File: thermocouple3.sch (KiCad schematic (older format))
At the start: 2 parts

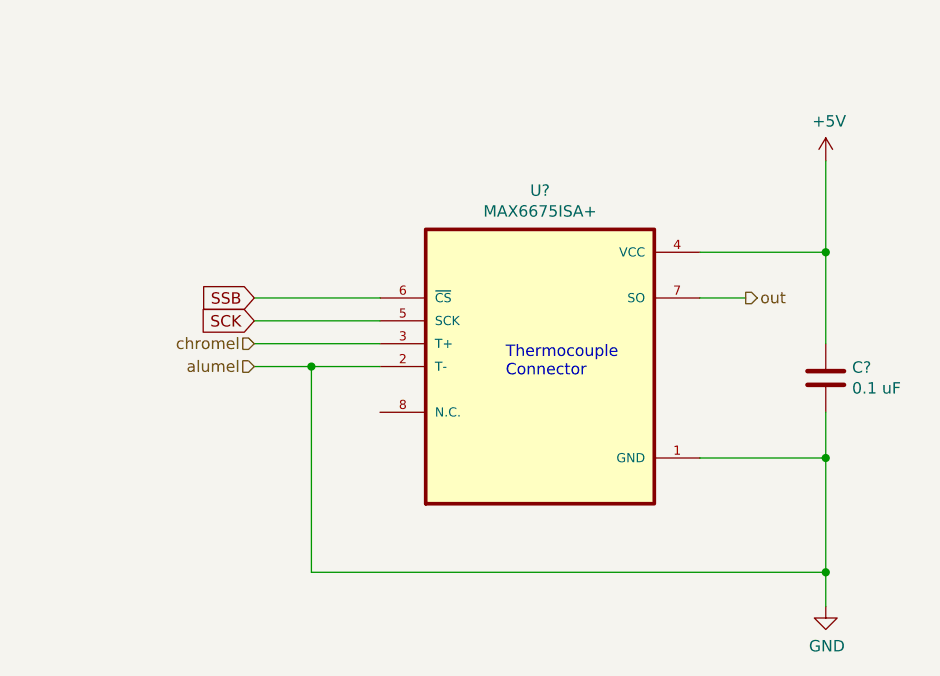
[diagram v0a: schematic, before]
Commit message: updated SCK
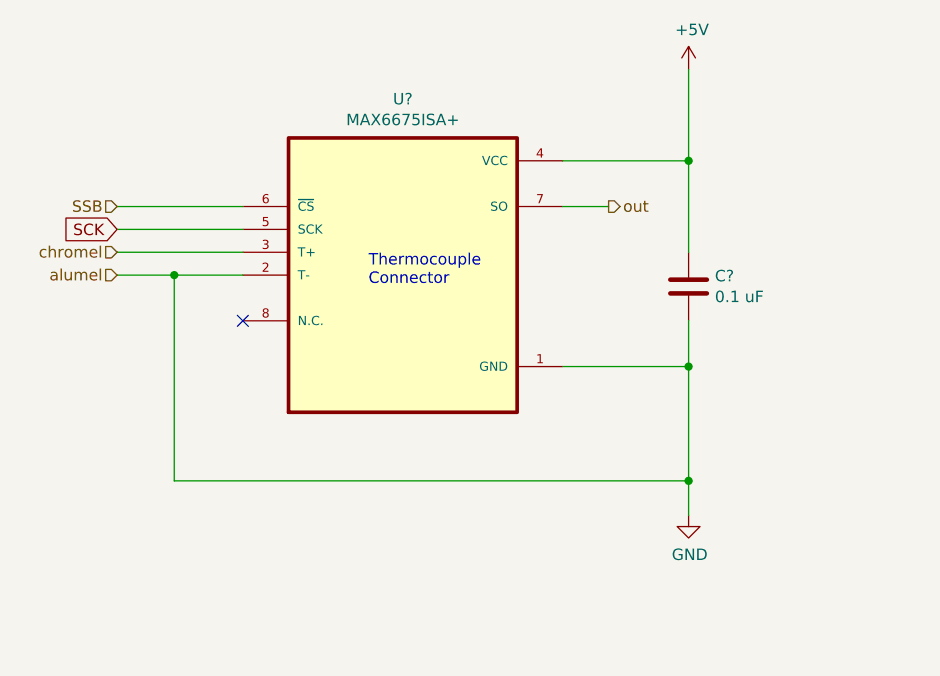
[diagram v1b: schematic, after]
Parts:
- removed C?: 0.1 uF, symbol Device:C
- removed U?: MAX6675ISA+, SOIC127P600X175-8N, symbol MAX6675ISA_:MAX6675ISA+
- added C?: 0.1 uF, symbol Device:C
- added U?: MAX6675ISA+, SOIC127P600X175-8N, symbol MAX6675ISA_:MAX6675ISA+
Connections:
- net +5V: now also C?.1, U?.4 (VCC)
- net GND: now also C?.2, U?.1 (GND), U?.2 (T-)
- net SCK: now also U?.5 (SCK)
- net SSB: now also U?.6 (~CS)
- net chromel: now also U?.3 (T+)
- net out: now also U?.7 (SO)
- no-connect marks 0 -> 1
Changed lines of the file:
@@
 Comment4 ""
 $EndDescr
-Text GLabel 4850 3650 0    50   Input ~ 0
-SCK
-Text GLabel 4850 3550 0    50   Input ~ 0
-SSB
-Connection ~ 7350 4250
+Connection ~ 6750 3850
 $Comp
 L MAX6675ISA_:MAX6675ISA+ U?
-U 1 1 604DF892
-P 6100 3850
-F 0 "U?" H 6100 4620 50  0000 C CNN
-F 1 "MAX6675ISA+" H 6100 4529 50  0000 C CNN
-F 2 "SOIC127P600X175-8N" H 6100 3850 50  0001 L BNN
-F 3 "" H 6100 3850 50  0001 L BNN
-	1    6100 3850
+U 1 1 60511F28
+P 5500 3450
+F 0 "U?" H 5500 4220 50  0000 C CNN
+F 1 "MAX6675ISA+" H 5500 4129 50  0000 C CNN
+F 2 "SOIC127P600X175-8N" H 5500 3450 50  0001 L BNN
+F 3 "" H 5500 3450 50  0001 L BNN
+	1    5500 3450
 	1    0    0    -1
 $EndComp
 Wire Wire Line
-	7350 4250 7350 4750
+	6750 3850 6750 4350
 Wire Wire Line
-	5100 4750 5100 3850
+	4500 4350 4500 3450
 Wire Wire Line
-	5100 3850 5400 3850
-Text Notes 5950 3900 0    50   ~ 0
+	4500 3450 4800 3450
+Text Notes 5350 3500 0    50   ~ 0
 Thermocouple\nConnector
 Wire Wire Line
-	4850 3850 5100 3850
-Connection ~ 5100 3850
+	4250 3450 4500 3450
+Connection ~ 4500 3450
 Wire Wire Line
-	5400 3750 4850 3750
+	4800 3350 4250 3350
 Wire Wire Line
-	6800 3350 7350 3350
+	6200 2950 6750 2950
 Wire Wire Line
-	6800 4250 7350 4250
+	6200 3850 6750 3850
 Wire Wire Line
-	5100 4750 7350 4750
+	4500 4350 6750 4350
 Wire Wire Line
-	6800 3550 7000 3550
+	6200 3150 6400 3150
 Wire Wire Line
-	4850 3650 5400 3650
+	4250 3250 4800 3250
 Wire Wire Line
-	5400 3550 4850 3550
+	4800 3150 4250 3150
 Wire Wire Line
-	7350 3350 7350 2950
-Connection ~ 7350 3350
+	6750 2950 6750 2550
+Connection ~ 6750 2950
 Wire Wire Line
-	7350 4750 7350 4900
-Connection ~ 7350 4750
+	6750 4350 6750 4500
+Connection ~ 6750 4350
 $Comp
 L power:GND #PWR?
-U 1 1 604DF8A9
-P 7350 4900
-F 0 "#PWR?" H 7350 4650 50  0001 C CNN
-F 1 "GND" H 7355 4727 50  0000 C CNN
-F 2 "" H 7350 4900 50  0001 C CNN
-F 3 "" H 7350 4900 50  0001 C CNN
-	1    7350 4900
+U 1 1 60511F3F
+P 6750 4500
+F 0 "#PWR?" H 6750 4250 50  0001 C CNN
+F 1 "GND" H 6755 4327 50  0000 C CNN
+F 2 "" H 6750 4500 50  0001 C CNN
+F 3 "" H 6750 4500 50  0001 C CNN
+	1    6750 4500
 	1    0    0    -1
 $EndComp
 $Comp
 L power:+5V #PWR?
-U 1 1 604DF8AF
-P 7350 2950
-F 0 "#PWR?" H 7350 2800 50  0001 C CNN
-F 1 "+5V" H 7365 3123 50  0000 C CNN
-F 2 "" H 7350 2950 50  0001 C CNN
-F 3 "" H 7350 2950 50  0001 C CNN
-	1    7350 2950
+U 1 1 60511F45
+P 6750 2550
+F 0 "#PWR?" H 6750 2400 50  0001 C CNN
+F 1 "+5V" H 6765 2723 50  0000 C CNN
+F 2 "" H 6750 2550 50  0001 C CNN
+F 3 "" H 6750 2550 50  0001 C CNN
+	1    6750 2550
 	1    0    0    -1
 $EndComp
 $Comp
 L Device:C C?
-U 1 1 604DF8B5
-P 7350 3900
-F 0 "C?" H 7465 3946 50  0000 L CNN
-F 1 "0.1 uF" H 7465 3855 50  0000 L CNN
-F 2 "" H 7388 3750 50  0001 C CNN
-F 3 "~" H 7350 3900 50  0001 C CNN
-	1    7350 3900
+U 1 1 60511F4B
+P 6750 3500
+F 0 "C?" H 6865 3546 50  0000 L CNN
+F 1 "0.1 uF" H 6865 3455 50  0000 L CNN
+F 2 "" H 6788 3350 50  0001 C CNN
+F 3 "~" H 6750 3500 50  0001 C CNN
+	1    6750 3500
 	1    0    0    -1
 $EndComp
 Wire Wire Line
-	7350 3350 7350 3750
+	6750 2950 6750 3350
 Wire Wire Line
-	7350 4050 7350 4250
-Text HLabel 7000 3550 2    50   Output ~ 0
+	6750 3650 6750 3850
+Text HLabel 6400 3150 2    50   Output ~ 0
 out
-Text HLabel 4850 3750 0    50   Input ~ 0
+Text HLabel 4250 3350 0    50   Input ~ 0
 chromel
-Text HLabel 4850 3850 0    50   Input ~ 0
+Text HLabel 4250 3450 0    50   Input ~ 0
 alumel
+Text HLabel 4250 3150 0    50   Input ~ 0
+SSB
+NoConn ~ 4800 3650
+Text GLabel 4250 3250 0    50   Input ~ 0
+SCK
 $EndSCHEMATC
